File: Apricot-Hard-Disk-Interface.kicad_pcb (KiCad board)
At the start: 2 copper layers, 132.4 x 58.4 mm, 23 parts, among them J1 Motherboard Connector, J2 Expansion, J3 SD_CARD_READER, P1 Pico, U1 GAL16V8, U2 74AHCT244, U3 74LS245, U4 GAL16V8, U5 74LS245, U6 74LS373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

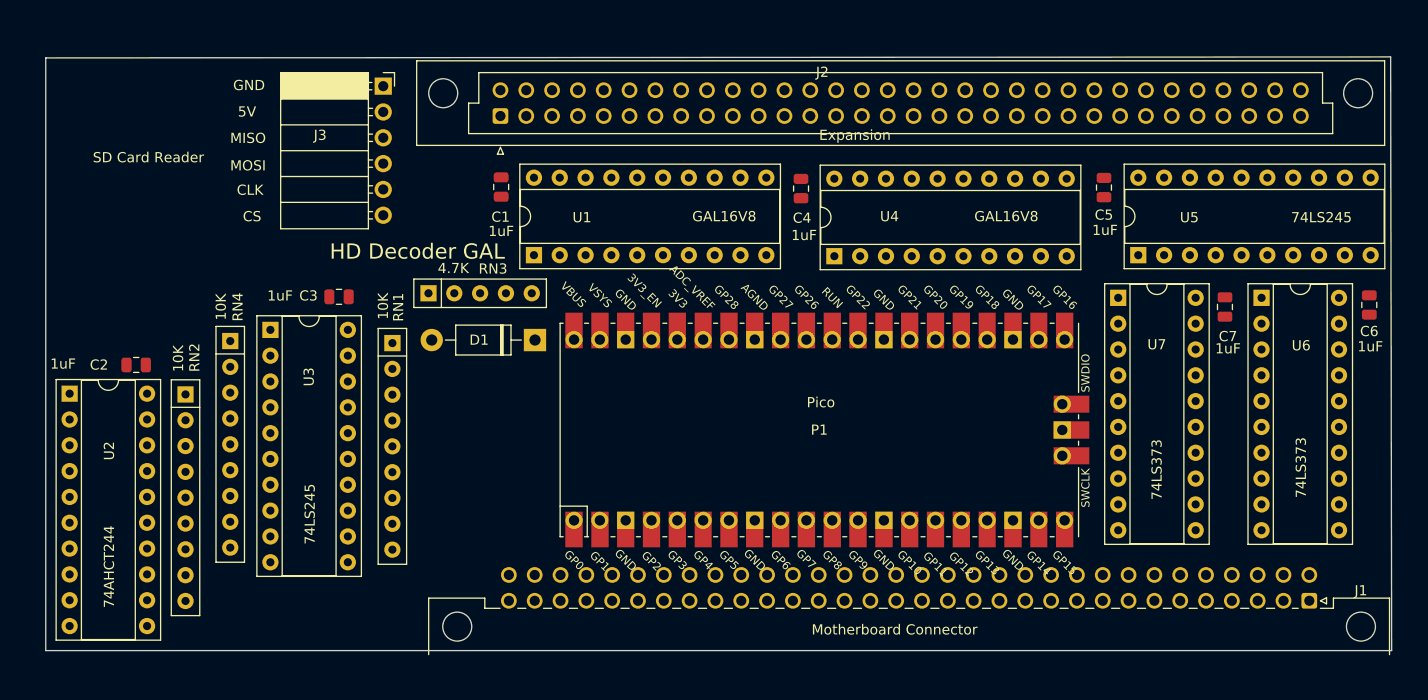
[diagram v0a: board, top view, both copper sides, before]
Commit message: Updated the PCB to the latest schematic and routed the PCB. Added Readme.md files
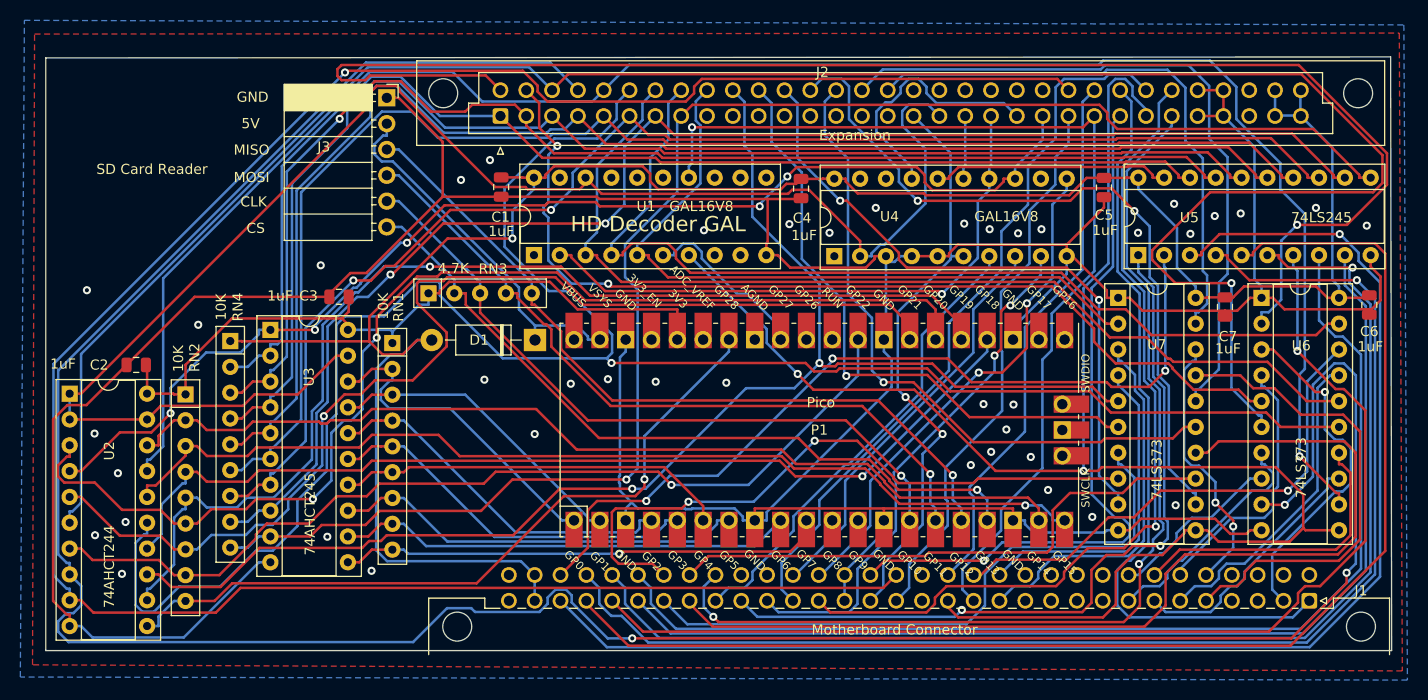
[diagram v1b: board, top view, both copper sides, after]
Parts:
- U3: value 74LS245 -> 74AHCT245
- moved J3 1.20 mm to (113.5, 82.9)
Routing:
- net GND: track 0.00 -> 392.5 mm, vias 0 -> 42
- net A1: track 0.00 -> 269.2 mm, vias 0 -> 3
- net IRDY: track 0.00 -> 222.6 mm, vias 0 -> 1
- net VCC: track 0.00 -> 217.1 mm, vias 0 -> 1
- net A0: track 0.00 -> 215.2 mm, vias 0 -> 1
- net A3: track 0.00 -> 196.7 mm, vias 0 -> 1
- net A2: track 0.00 -> 183.6 mm, vias 0 -> 1
- net ALE: track 0.00 -> 166.1 mm, vias 0 -> 2
- net _SELECTED: track 0.00 -> 156.1 mm
- net D7: track 0.00 -> 152.5 mm, vias 0 -> 1
- net _I_BHE: track 0.00 -> 149.8 mm, vias 0 -> 1
- net D6: track 0.00 -> 139.6 mm, vias 0 -> 2
- net D4: track 0.00 -> 137.6 mm
- net A7: track 0.00 -> 137.3 mm, vias 0 -> 2
- net DB1: track 0.00 -> 136.5 mm, vias 0 -> 1
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- added copper zone on B.Cu, net GND
- added copper zone on F.Cu, net GND
